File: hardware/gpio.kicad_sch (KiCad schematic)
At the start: 6 parts, among them J8 Conn_01x03, J9 Conn_02x20_Odd_Even, Q4 BSN20

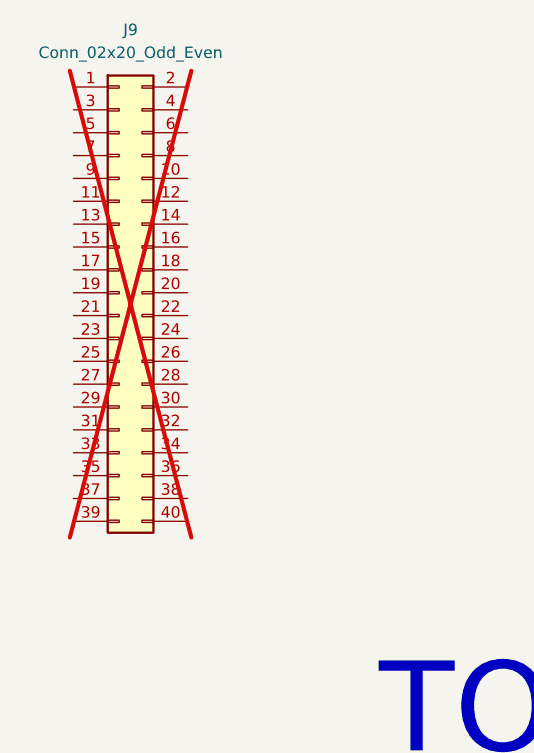
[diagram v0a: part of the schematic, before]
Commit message: Laid out the DCDC bucks
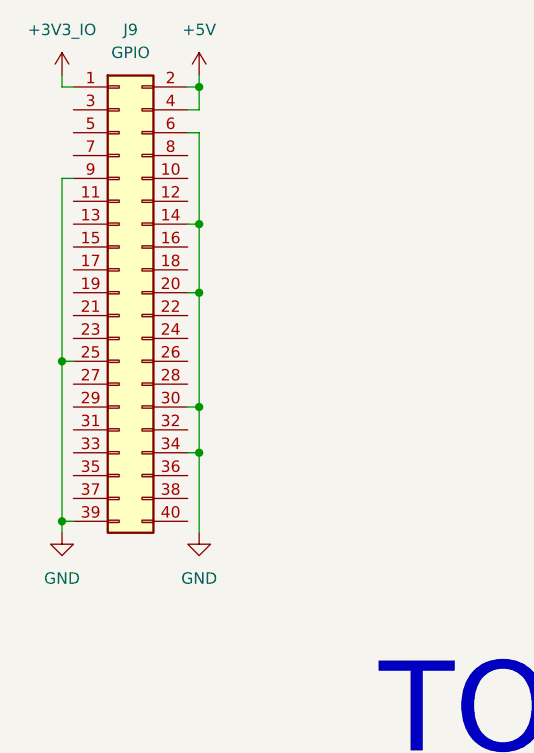
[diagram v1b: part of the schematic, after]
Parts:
- J9: value Conn_02x20_Odd_Even -> GPIO; now fitted
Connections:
- net +3V3_IO: now also J9.1 (Pin_1)
- net GND: now also J9.14 (Pin_14), J9.20 (Pin_20), J9.25 (Pin_25), J9.30 (Pin_30), J9.34 (Pin_34), J9.39 (Pin_39), J9.6 (Pin_6), J9.9 (Pin_9)
- net +5V: now reaches J9.2 (Pin_2)
- net +5V: now also J9.4 (Pin_4)

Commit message: Even more routing
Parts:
- added D3, D4: LED, symbol Device:LED
- added R71, R72: 2k, Resistor_SMD:R_0402_1005Metric, symbol Device:R
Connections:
- net GND: now also D3.1 (K), D4.1 (K)
- new net: D4.2 (A), R72.1
- new net: D3.2 (A), R71.1
- new net PWR_LED: R71.2
- new net STATUS_LED: R72.2
